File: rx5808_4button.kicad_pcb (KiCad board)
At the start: 2 copper layers, 80 x 65 mm, 61 parts, among them IC1 ATMEGA328-A, P1 CONN_01X02, P10 CONN_01X01, P11 CONN_01X01, P2 CONN_01X05, P3 CONN_02X03, P4 CONN_01X02, P5 BNC, P6 BNC, P7 CONN_01X02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

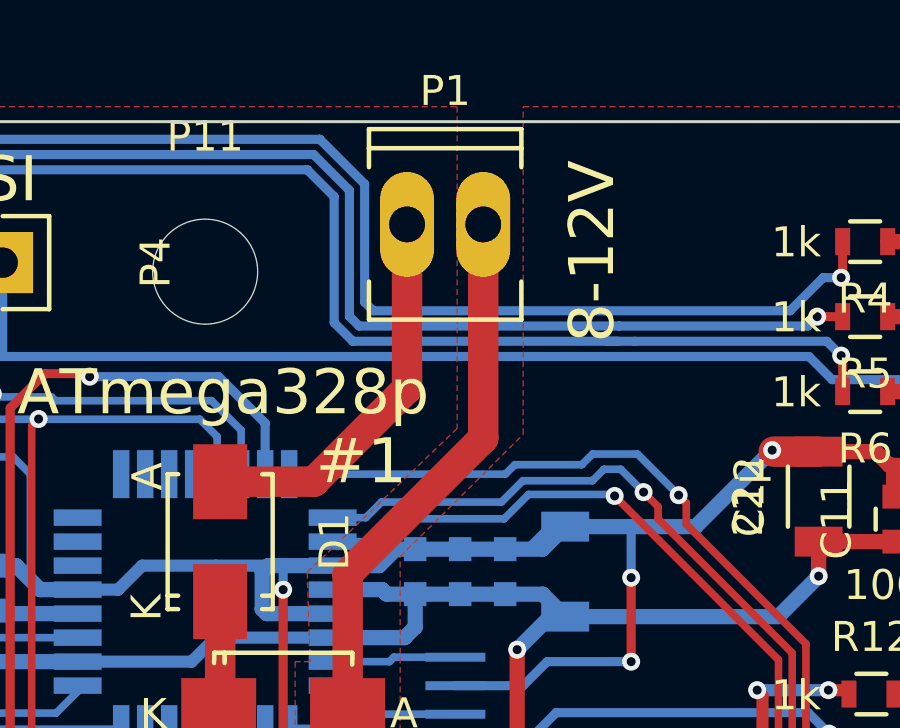
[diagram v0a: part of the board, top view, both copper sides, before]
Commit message: SMA-buchse richtig gestellt
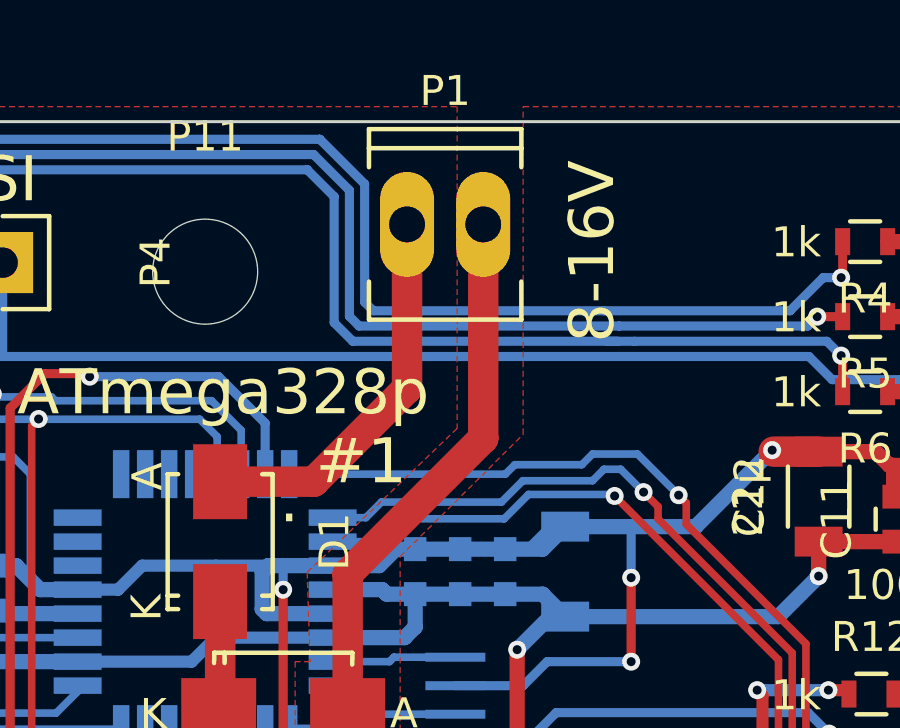
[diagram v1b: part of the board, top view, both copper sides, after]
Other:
- board text added: "."
- board text added: "8-16V"
- board text removed: "8-12V"

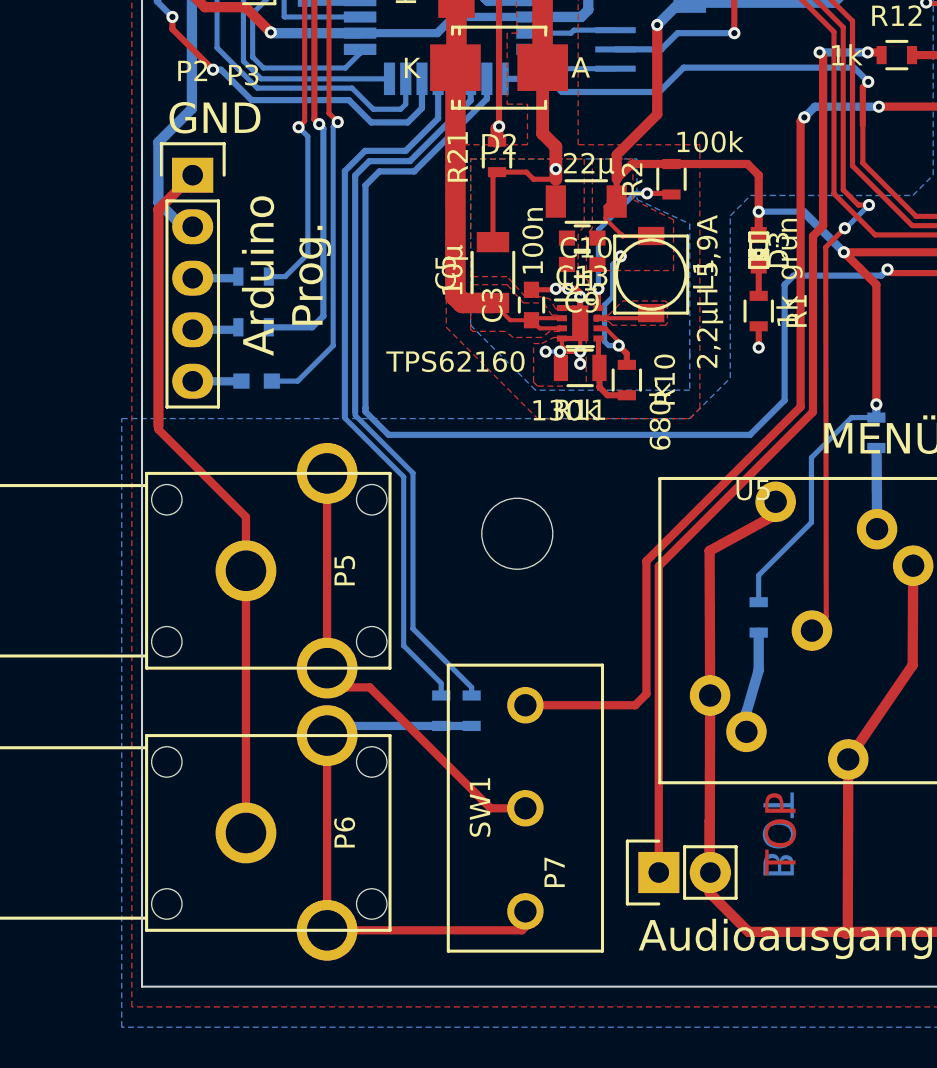
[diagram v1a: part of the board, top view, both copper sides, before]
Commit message: 130k-Ohm durch zwei parallele Widerstände ersetzt, um eine vollständige E12-Kompatibilität gewährleisten zu können
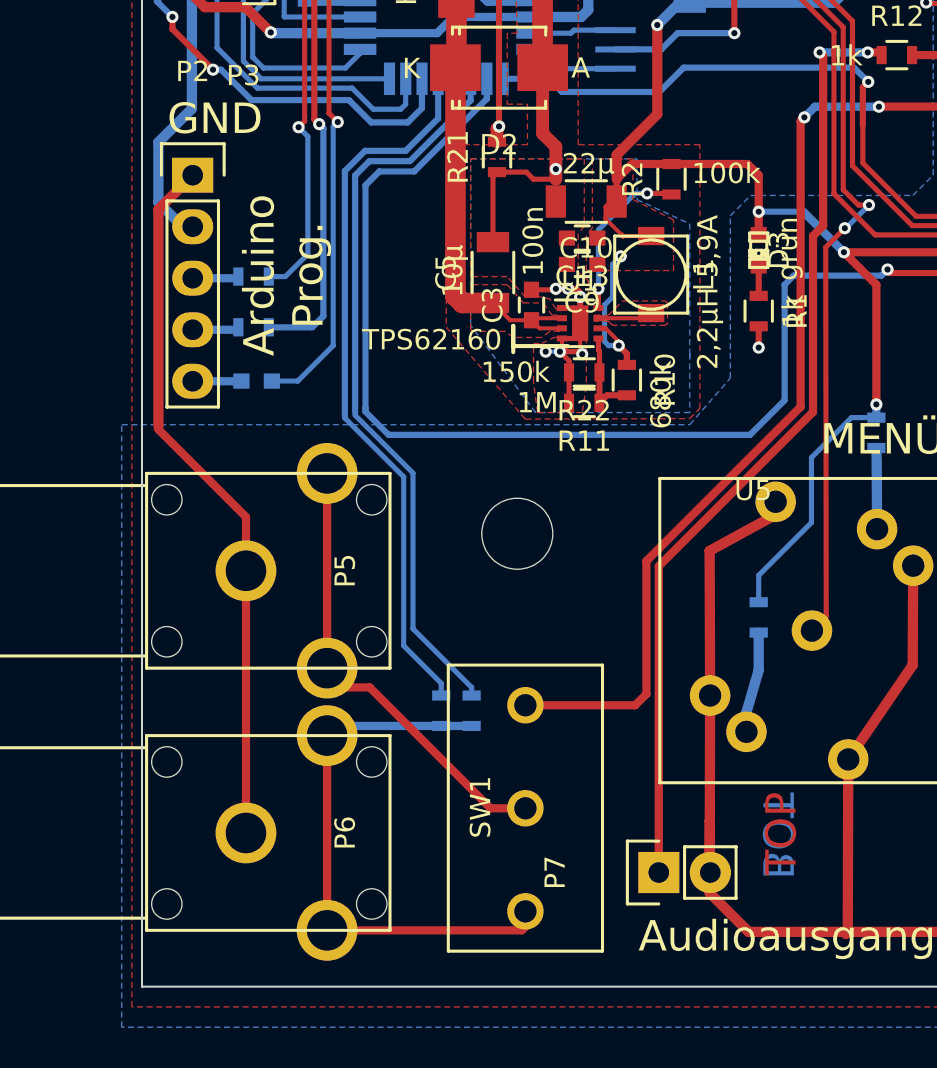
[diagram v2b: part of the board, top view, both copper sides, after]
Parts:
- added R22: 150k, Resistors_SMD:R_0603, F.Cu at (105.8, 113.9)
- R11: value 130k -> 1M; footprint Resistors_SMD:R_0805 -> Resistors_SMD:R_0603
- moved R11 1.74 mm to (105.8, 115.4)
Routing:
- net GNDPWR: track 41.7 -> 44.9 mm, vias 8 -> 7
- net Net-(R10-Pad2): track 3.94 -> 4.70 mm
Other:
- rule pad_to_mask_clearance: 0.1 -> 0.15
